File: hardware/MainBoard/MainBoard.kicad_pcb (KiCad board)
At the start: 2 copper layers, 38.1 x 73.8 mm, 50 parts, among them J1 Conn_01x08_Socket, J2 Conn_01x08_Socket, J3 Conn_01x08_Socket, J4 Micro_SD_Card_Det2, J5 USB_C_Receptacle_USB2.0_16P, J8 En_A, J9 En_B, Q1 MMBT2222A, U1 ESP32-S3-WROOM-1, U2 AMS1117-3.3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

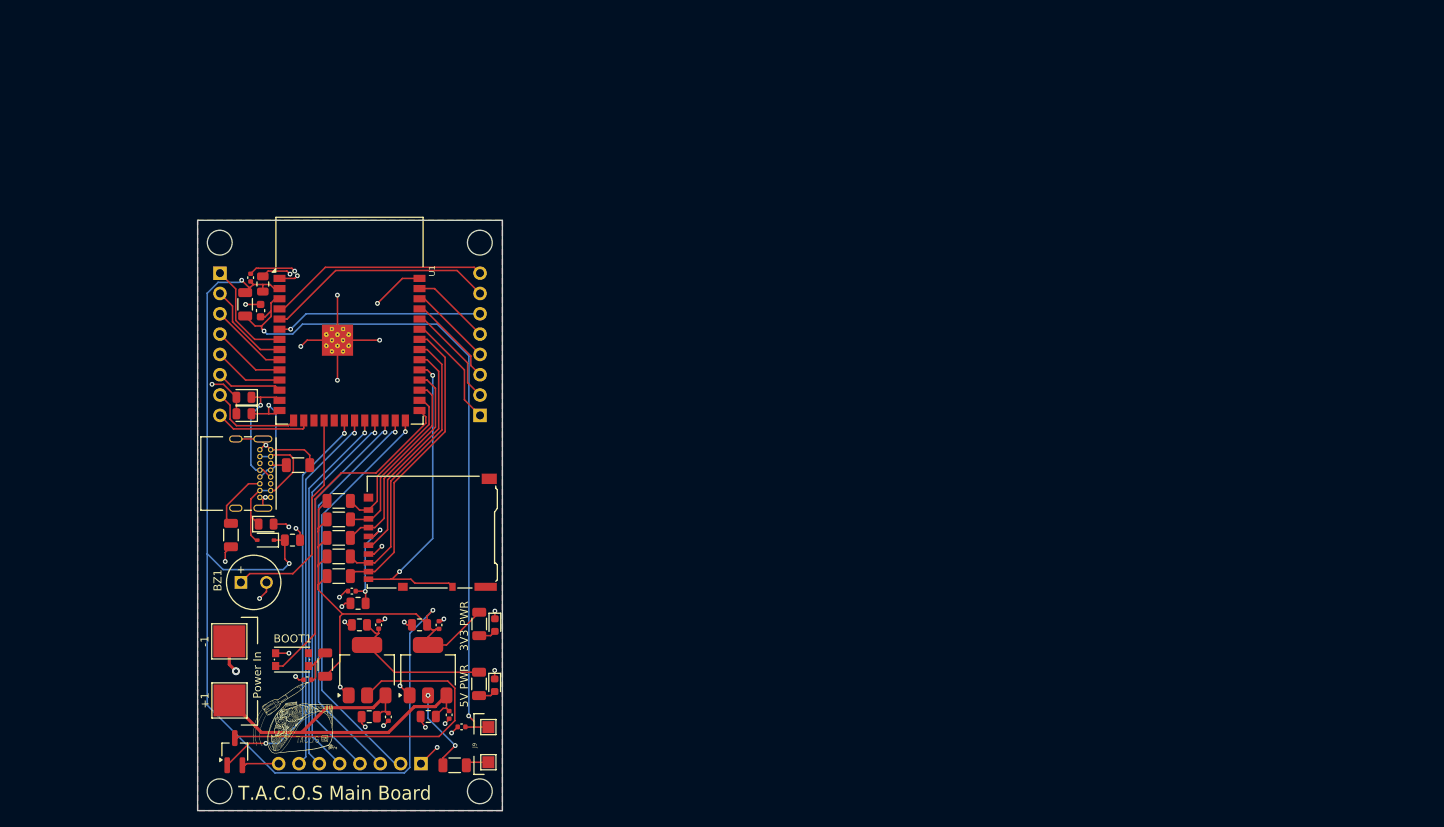
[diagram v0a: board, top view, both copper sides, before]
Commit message: designing new main board
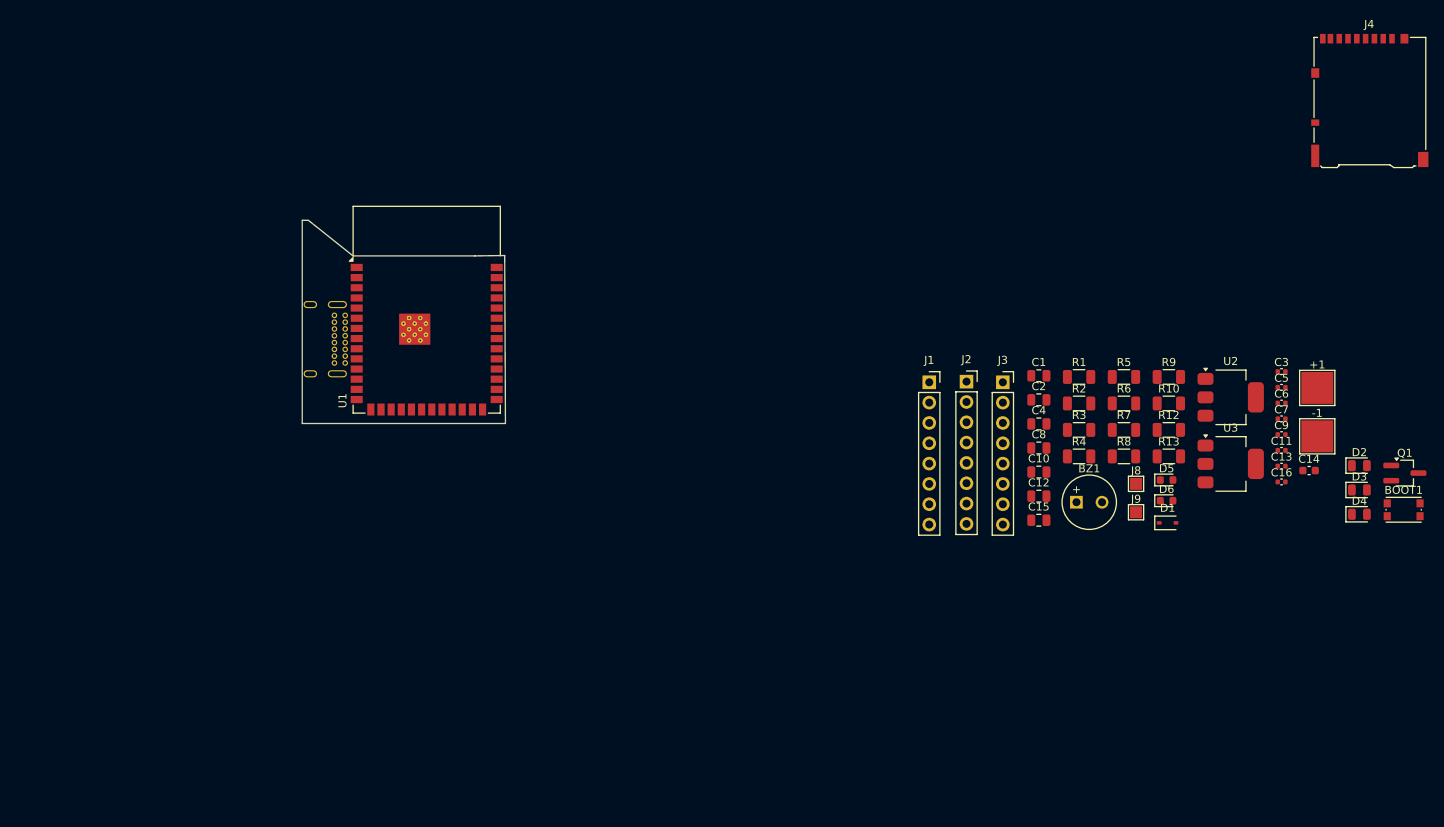
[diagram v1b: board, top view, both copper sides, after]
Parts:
- removed G***: LOGO, lib:tacos_logo
- J1, J2, J3: moved to F.Cu
- J5: moved to B.Cu
- moved Q1 150.3 mm to (201.7, 82.4), turned to 0 degrees
- moved +1 141.5 mm to (190.8, 71.8), turned to 0 degrees
- moved BOOT1 140.2 mm to (201.6, 87.0)
- moved D4 140.0 mm to (196.0, 87.5), turned to 0 degrees
- moved D3 139.9 mm to (196.0, 84.5), turned to 0 degrees
- moved -1 138.4 mm to (190.8, 77.8), turned to 0 degrees
- moved D2 136.9 mm to (196.0, 81.5)
- moved C14 132.6 mm to (189.7, 82.1), turned to 0 degrees
- moved C16 131.4 mm to (186.3, 83.5), turned to 0 degrees
- moved J4 129.2 mm to (197.3, 35.8), turned to 0 degrees
- moved C6 126.6 mm to (186.3, 73.7), turned to 0 degrees
- moved C13 117.3 mm to (186.3, 81.5), turned to 0 degrees
- moved C9 117.1 mm to (186.3, 77.6), turned to 0 degrees
- moved C11 115.0 mm to (186.3, 79.6), turned to 0 degrees
- moved D1 112.8 mm to (172.1, 88.6), turned to 0 degrees
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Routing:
- net ESP_3V3: track 211.4 -> 0.00 mm, vias 7 -> 0
- net LIPO GND: track 100.1 -> 0.00 mm, vias 36 -> 0
- net CHIP_PU: track 87.1 -> 0.00 mm, vias 2 -> 0
- net VCC_5V: track 64.5 -> 0.00 mm
- net HATS_ENABLE: track 52.0 -> 0.00 mm, vias 2 -> 0
- net I0: track 51.7 -> 0.00 mm, vias 1 -> 0
- net LIPO PWR: track 50.6 -> 0.00 mm
- net I1: track 50.3 -> 0.00 mm, vias 1 -> 0
- net I2: track 49.0 -> 0.00 mm, vias 1 -> 0
- net GPIO0: track 48.6 -> 0.00 mm
- net I3: track 47.8 -> 0.00 mm, vias 1 -> 0
- net I4: track 46.3 -> 0.00 mm, vias 1 -> 0
- net SELECT RETURN: track 46.0 -> 0.00 mm, vias 1 -> 0
- net SD_DET: track 40.6 -> 0.00 mm, vias 2 -> 0
- net SD_DAT1: track 37.8 -> 0.00 mm
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- removed copper zone on B.Cu, net LIPO GND
- removed copper zone on F.Cu, net LIPO GND
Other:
- board size 38.1 x 73.8 mm -> 25.4 x 25.4 mm
- board text removed: "3V3 PWR"
- board text removed: "5V PWR"
- board text removed: "Power In"
- board text removed: "T.A.C.O.S Main Board"

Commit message: main boards almost done:
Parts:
- removed J2, J3: Conn_01x08_Socket, Connector_PinSocket_2.54mm:PinSocket_1x08_P2.54mm_Vertical
- added Hat_Conn1: Conn_02x15_Top_Bottom, Connector_Molex:Molex_SlimStack_53748-0308_2x15_P0.50mm_Vertical, F.Cu at (82.8, 89.2)
- added Plug1: Conn_02x15_Top_Bottom, Connector_Molex:Molex_SlimStack_53748-0308_2x15_P0.50mm_Vertical, F.Cu at (80.3, 70.6)
- added Recepticle1: Conn_02x15_Top_Bottom, Connector_Molex:Molex_SlimStack_53748-0308_2x15_P0.50mm_Vertical, B.Cu at (80.3, 104.6)
- +1, -1: footprint TestPoint:TestPoint_Pad_4.0x4.0mm -> TestPoint:TestPoint_Pad_2.0x2.0mm; moved to B.Cu
- BOOT1, C11, C6, C7, C9, D5, J8, J9, U1, U3: moved to B.Cu
- BZ1: footprint Buzzer_Beeper:MagneticBuzzer_Kingstate_KCG0601 -> Buzzer_Beeper:Buzzer_Murata_PKMCS0909E; moved to B.Cu
- C1, C12, C15, C2, C4: footprint Capacitor_SMD:C_0805_2012Metric -> Capacitor_SMD:C_0603_1608Metric
- C10, C8: footprint Capacitor_SMD:C_0805_2012Metric -> Capacitor_SMD:C_0603_1608Metric; moved to B.Cu
- D2: footprint Diode_SMD:D_0805_2012Metric -> Diode_SMD:D_0603_1608Metric
- D3, D4: footprint Diode_SMD:D_0805_2012Metric -> Diode_SMD:D_0603_1608Metric; moved to B.Cu
- J1: value Conn_01x08_Socket -> Conn_01x01; footprint Connector_PinSocket_2.54mm:PinSocket_1x08_P2.54mm_Vertical -> TestPoint:TestPoint_Pad_1.5x1.5mm
- J5: moved to F.Cu
- Q1: footprint Package_TO_SOT_SMD:SOT-23W_Handsoldering -> Package_TO_SOT_SMD:SOT-23W; moved to B.Cu
- R1, R2: footprint Resistor_SMD:R_1206_3216Metric -> Resistor_SMD:R_0402_1005Metric
- R10, R12, R13, R4, R5, R6, R8, R9: footprint Resistor_SMD:R_1206_3216Metric -> Resistor_SMD:R_0603_1608Metric; moved to B.Cu
- R3, R7: footprint Resistor_SMD:R_1206_3216Metric -> Resistor_SMD:R_0603_1608Metric
- moved BOOT1 137.7 mm to (65.7, 64.6), turned to -90 degrees
- moved J4 133.1 mm to (81.4, 101.3)
- moved +1 129.3 mm to (65.7, 104.3), turned to 180 degrees
- moved -1 128.8 mm to (65.7, 108.4), turned to 180 degrees
- moved D3 128.5 mm to (69.0, 104.0), turned to 180 degrees
- moved D4 128.3 mm to (69.0, 105.7), turned to 180 degrees
- moved C14 126.2 mm to (65.5, 60.2), turned to 180 degrees
- moved Q1 125.8 mm to (77.2, 100.0), turned to 180 degrees
- moved D2 125.2 mm to (72.0, 98.6)
- moved C6 122.6 mm to (64.4, 60.8), turned to 90 degrees
- moved C7 121.0 mm to (65.3, 72.6), turned to 180 degrees
- moved C9 120.9 mm to (67.9, 101.8), turned to 90 degrees
- moved C11 116.0 mm to (70.8, 90.2), turned to 90 degrees
- moved C13 115.6 mm to (71.5, 95.5), turned to 180 degrees
- moved U3 113.2 mm to (67.6, 95.7), turned to 90 degrees
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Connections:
- net ESP_3V3 renamed CONN_26
- net HATS_ENABLE renamed CONN_12
- net SD_CLK renamed CONN_4
- net SD_CMD renamed CONN_6
- net SD_DAT0 renamed CONN_2
- net SD_DAT1 renamed CONN_0
- net SD_DAT2 renamed CONN_10
- net SD_DAT3 renamed CONN_8
- net USB+ renamed CONN_3
- net USB- renamed CONN_1
- J1 pad 1: LIPO GND -> CONN_5V
- Q1 pad 2: Net-(J1-Pin_8) -> CONN_5V
- U1 pad 10: DATA11 -> unconnected-(U1-IO17-Pad10)
- U1 pad 11: DATA12 -> unconnected-(U1-IO18-Pad11)
- U1 pad 12: DATA13 -> unconnected-(U1-IO8-Pad12)
- U1 pad 15: DATA14 -> unconnected-(U1-IO3-Pad15)
- U1 pad 16: DATA15 -> unconnected-(U1-IO46-Pad16)
- U1 pad 21: SELECT RETURN -> RET
- U1 pad 22: I4 -> unconnected-(U1-IO14-Pad22)
- U1 pad 23: I3 -> unconnected-(U1-IO21-Pad23)
- U1 pad 24: I2 -> unconnected-(U1-IO47-Pad24)
- U1 pad 25: I1 -> unconnected-(U1-IO48-Pad25)
- U1 pad 26: I0 -> unconnected-(U1-IO45-Pad26)
- U1 pad 35: DATA7 -> unconnected-(U1-IO42-Pad35)
- U1 pad 36: DATA6 -> unconnected-(U1-RXD0-Pad36)
- U1 pad 37: DATA5 -> unconnected-(U1-TXD0-Pad37)
- U1 pad 38: DATA4 -> unconnected-(U1-IO2-Pad38)
- U1 pad 39: DATA3 -> unconnected-(U1-IO1-Pad39)
- U1 pad 4: DATA0 -> unconnected-(U1-IO4-Pad4)
- U1 pad 5: DATA1 -> unconnected-(U1-IO5-Pad5)
- U1 pad 6: DATA2 -> unconnected-(U1-IO6-Pad6)
- U1 pad 7: DATA8 -> unconnected-(U1-IO7-Pad7)
- U1 pad 8: DATA9 -> unconnected-(U1-IO15-Pad8)
- U1 pad 9: DATA10 -> unconnected-(U1-IO16-Pad9)
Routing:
- net SD_DET: track 0.00 -> 10.9 mm, vias 0 -> 2
- net Net-(D6-A): track 0.00 -> 3.30 mm, vias 0 -> 1
- net LIPO GND: track 0.00 -> 3.10 mm, vias 0 -> 3
- net Net-(D5-A): track 0.00 -> 1.97 mm, vias 0 -> 1
- net CONN_3: track 0.00 -> 1.70 mm, vias 0 -> 1
- net CONN_1: track 0.00 -> 1.70 mm, vias 0 -> 1
- net CONN_0: track 0.00 -> 1.32 mm, vias 0 -> 2
- net CONN_4: track 0.00 -> 1.22 mm, vias 0 -> 2
- net CONN_26: track 0.00 -> 1.21 mm, vias 0 -> 6
- net CONN_2: track 0.00 -> 1.21 mm, vias 0 -> 2
- net CONN_8: track 0.00 -> 1.17 mm, vias 0 -> 2
- net CONN_6: track 0.00 -> 1.13 mm, vias 0 -> 2
- net CONN_10: track 0.00 -> 1.11 mm, vias 0 -> 2
- net (no net): track 0.00 -> 0.31 mm, vias 0 -> 20
- net unconnected-(U1-IO9-Pad17): vias 0 -> 1
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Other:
- board size 25.4 x 25.4 mm -> 25.4 x 59.4 mm

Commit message: started wiring main boards
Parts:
- removed the C1 at (65.6, 98.8)
- removed the C2 at (76.2, 67.1)
- removed the C3 at (78.5, 66.8)
- removed R13: 10k, Resistor_SMD:R_0603_1608Metric
- added C12: 10uF, Capacitor_SMD:C_0603_1608Metric, F.Cu at (65.6, 98.8)
- added C13: 10uF, Capacitor_SMD:C_0603_1608Metric, B.Cu at (77.4, 96.7)
- added C14: 0u1F, Capacitor_SMD:C_0402_1005Metric, B.Cu at (64.9, 59.6)
- added C15: 100nF, Capacitor_SMD:C_0402_1005Metric, B.Cu at (78.6, 97.2)
- added C16: 0u1F, Capacitor_SMD:C_0402_1005Metric, B.Cu at (65.3, 72.6)
- added G***: LOGO, lib:tacos_logo, F.Cu at (72.2, 81.1)
- added J10: Conn_01x01, TestPoint:TestPoint_Pad_1.5x1.5mm, B.Cu at (75.8, 104.6)
- added J2: Conn_01x01, TestPoint:TestPoint_Pad_1.5x1.5mm, F.Cu at (78.2, 89.1)
- added J3: USB_C_Receptacle_USB2.0_16P, Connector_USB:USB_C_Receptacle_GCT_USB4085, F.Cu at (72.5, 101.9)
- added J6: Micro_SD_Card_Det2, Connector_Card:microSD_HC_Hirose_DM3AT-SF-PEJM5, F.Cu at (81.4, 101.3)
- added J7: Conn_01x01, TestPoint:TestPoint_Pad_1.5x1.5mm, F.Cu at (85.1, 70.7)
- added R11: 10k, Resistor_SMD:R_0603_1608Metric, B.Cu at (86.1, 100.3)
- added R2: 75, Resistor_SMD:R_0603_1608Metric, F.Cu at (65.4, 56.3)
- added R7: 10k, Resistor_SMD:R_0603_1608Metric, B.Cu at (81.5, 100.3)
- C6: value 0u1F -> 10uF; footprint Capacitor_SMD:C_0402_1005Metric -> Capacitor_SMD:C_0603_1608Metric; moved to F.Cu
- C7, D3: moved to F.Cu
- D1: value 1N5819WS -> PWRLED; footprint Diode_SMD:D_SOD-323 -> LED_SMD:LED_0603_1608Metric; moved to B.Cu
- D2: value D_TVS_Small_Filled -> PWRLED; footprint Diode_SMD:D_0603_1608Metric -> LED_SMD:LED_0603_1608Metric
- D4: value D_TVS_Small_Filled -> 1N5819WS; footprint Diode_SMD:D_0603_1608Metric -> Diode_SMD:D_SOD-323; moved to F.Cu
- D5: value PWRLED -> D_TVS_Small_Filled; footprint LED_SMD:LED_0603_1608Metric -> Diode_SMD:D_0603_1608Metric
- D6: value PWRLED -> D_TVS_Small_Filled; footprint LED_SMD:LED_0603_1608Metric -> Diode_SMD:D_0603_1608Metric; moved to B.Cu
- J4: value Micro_SD_Card_Det2 -> En_A; footprint Connector_Card:microSD_HC_Hirose_DM3AT-SF-PEJM5 -> TestPoint:TestPoint_Pad_1.5x1.5mm; moved to B.Cu
- J5: value USB_C_Receptacle_USB2.0_16P -> En_B; footprint Connector_USB:USB_C_Receptacle_GCT_USB4085 -> TestPoint:TestPoint_Pad_1.5x1.5mm; moved to B.Cu
- J8: value En_A -> Conn_01x01; moved to F.Cu
- J9: value En_B -> Conn_01x01
- R3: moved to B.Cu
- R4, R5: value 10k -> 5k1; footprint Resistor_SMD:R_0603_1608Metric -> Resistor_SMD:R_0402_1005Metric
- R6: value 75 -> 10k
- moved D5 47.8 mm to (69.0, 104.0), turned to 180 degrees
- moved R4 46.9 mm to (68.4, 107.0), turned to 180 degrees
- moved R10 43.1 mm to (65.5, 60.9), turned to 180 degrees
- moved D1 42.4 mm to (65.4, 56.3)
- moved J9 35.9 mm to (84.9, 104.7)
- moved R12 35.6 mm to (65.5, 68.5), turned to 180 degrees
- moved J4 34.2 mm to (65.6, 70.9), turned to 180 degrees
- moved R5 33.9 mm to (68.4, 102.6)
- moved R3 33.9 mm to (65.7, 90.2), turned to 180 degrees
- moved J5 28.3 mm to (65.6, 74.4), turned to 180 degrees
- moved R6 20.0 mm to (83.0, 100.3), turned to -90 degrees
- moved D6 19.9 mm to (69.0, 105.7), turned to 180 degrees
- moved C7 18.6 mm to (79.2, 60.2), turned to 0 degrees
- moved C6 15.4 mm to (79.8, 61.5), turned to 0 degrees
- moved D2 14.4 mm to (64.7, 86.3), turned to -90 degrees
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- renumbered C14 to C1, C16 to C2, C15 to C3, R7 to R1
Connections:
- +1 pad 1: LIPO PWR -> CONN_3V
- C4 pad 1: CONN_26 -> CONN_3V
- C5 pad 1: CONN_26 -> CONN_3V
- C6 pad 1: GPIO0 -> CONN_26
- C7 pad 1: CHIP_PU -> CONN_26
- C8 pad 1: LIPO PWR -> CONN_3V
- C9 pad 1: LIPO PWR -> CONN_3V
- D1 pad 1: CONN_26 -> LIPO GND
- D2 pad 1: Net-(D1-A) -> LIPO GND
- D2 pad 2: LIPO GND -> Net-(D2-A)
- D3 pad 1: CONN_1 -> Net-(D3-A1)
- D4 pad 1: CONN_3 -> CONN_26
- D4 pad 2: LIPO GND -> Net-(D3-A1)
- D5 pad 1: LIPO GND -> CONN_1
- D5 pad 2: Net-(D5-A) -> LIPO GND
- D6 pad 1: LIPO GND -> CONN_3
- D6 pad 2: Net-(D6-A) -> LIPO GND
- Hat_Conn1 pad 30: unconnected-(Hat_Conn1-Pin_30-Pad30) -> RET
- J4 pad 1: CONN_10 -> Net-(J4-Pin_1)
- J8 pad 1: Net-(J8-Pin_1) -> CONN_GND
- J9 pad 1: CHIP_PU -> CONN_3V
- Plug1 pad 29: RET -> CONN_27
- R10 pad 2: CONN_6 -> GPIO0
- R12 pad 2: CONN_2 -> Net-(J4-Pin_1)
- R3 pad 1: CONN_26 -> VCC_5V
- R3 pad 2: Net-(D5-A) -> Net-(D2-A)
- R4 pad 1: CONN_26 -> Net-(J3-CC2)
- R4 pad 2: GPIO0 -> LIPO GND
- R5 pad 1: CONN_26 -> Net-(J3-CC1)
- R5 pad 2: Net-(J8-Pin_1) -> LIPO GND
- R6 pad 1: VCC_5V -> CONN_26
- R6 pad 2: Net-(D6-A) -> CONN_6
- R8 pad 2: CONN_10 -> CONN_8
- R9 pad 2: CONN_8 -> CONN_0
- U1 pad 27: GPIO0 -> unconnected-(U1-IO0-Pad27)
- U1 pad 39: unconnected-(U1-IO1-Pad39) -> GPIO0
- U2 pad 3: LIPO PWR -> CONN_3V
- U3 pad 3: LIPO PWR -> CONN_3V
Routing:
- net CONN_26: track 1.21 -> 30.5 mm, vias 6 -> 11
- net CHIP_PU: track 0.00 -> 28.8 mm
- net CONN_3V: track 0.00 -> 23.3 mm
- net GPIO0: track 0.00 -> 19.6 mm
- net LIPO GND: track 3.10 -> 15.8 mm, vias 3 -> 14
- net Net-(D6-A): track 3.30 -> 0.00 mm, vias 1 -> 0
- net Net-(D2-A): track 0.00 -> 1.98 mm, vias 0 -> 1
- net Net-(D5-A): track 1.97 -> 0.00 mm, vias 1 -> 0
- net Net-(D1-A): track 0.00 -> 1.97 mm, vias 0 -> 1
- net CONN_27: track 0.00 -> 1.60 mm, vias 0 -> 4
- net CONN_9: track 0.00 -> 0.82 mm, vias 0 -> 2
- net CONN_23: track 0.00 -> 0.82 mm, vias 0 -> 2
- net CONN_22: track 0.00 -> 0.82 mm, vias 0 -> 2
- net CONN_3: track 1.70 -> 2.51 mm, vias 1 -> 3
- net CONN_7: track 0.00 -> 0.81 mm, vias 0 -> 2
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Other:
- copper layers 2 -> 4

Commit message: wide board lel
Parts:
- removed Hat_Conn1, Plug1, Recepticle1: Conn_02x15_Top_Bottom, Connector_Molex:Molex_SlimStack_53748-0308_2x15_P0.50mm_Vertical
- removed J10, J8, J9: Conn_01x01, TestPoint:TestPoint_Pad_1.5x1.5mm
- J1: value Conn_01x01 -> Conn_02x16_Top_Bottom; footprint TestPoint:TestPoint_Pad_1.5x1.5mm -> MolexFSB:FSB5 Series 0.40 mm Pitch Floating SlimStack Board-to-Board Receptacles; moved to B.Cu
- J2, J7: value Conn_01x01 -> Conn_02x16_Top_Bottom; footprint TestPoint:TestPoint_Pad_1.5x1.5mm -> MolexFSB:FSB5 Series 0.40 mm Pitch Floating SlimStack Board-to-Board Plugs
- moved J7 19.3 mm to (80.3, 89.4)
- moved J2 18.6 mm to (80.3, 70.6), turned to 180 degrees
- moved J1 16.9 mm to (80.3, 104.6), turned to 180 degrees
- moved BZ1 0.20 mm to (83.9, 91.2)
- turned R11 to -90 degrees
- turned R8 to -90 degrees
- turned R9 to -90 degrees
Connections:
- -1 pad 1: LIPO GND -> CONN_GND
- BOOT1 pad 1: LIPO GND -> CONN_GND
- BZ1 pad 2: LIPO GND -> CONN_GND
- C1 pad 2: LIPO GND -> CONN_GND
- C10 pad 2: LIPO GND -> CONN_GND
- C11 pad 2: LIPO GND -> CONN_GND
- C12 pad 1: CONN_26 -> CONN_VCC
- C12 pad 2: LIPO GND -> CONN_GND
- C13 pad 1: CONN_26 -> CONN_VCC
- C13 pad 2: LIPO GND -> CONN_GND
- C14 pad 2: LIPO GND -> CONN_GND
- C15 pad 1: CONN_26 -> CONN_VCC
- C15 pad 2: LIPO GND -> CONN_GND
- C16 pad 2: LIPO GND -> CONN_GND
- C2 pad 1: CONN_26 -> CONN_VCC
- C2 pad 2: LIPO GND -> CONN_GND
- C3 pad 1: CONN_26 -> CONN_VCC
- C3 pad 2: LIPO GND -> CONN_GND
- C4 pad 2: LIPO GND -> CONN_GND
- C5 pad 2: LIPO GND -> CONN_GND
- C6 pad 1: CONN_26 -> CONN_VCC
- C6 pad 2: LIPO GND -> CONN_GND
- C7 pad 1: CONN_26 -> CONN_VCC
- C7 pad 2: LIPO GND -> CONN_GND
- C8 pad 2: LIPO GND -> CONN_GND
- C9 pad 2: LIPO GND -> CONN_GND
- D1 pad 1: LIPO GND -> CONN_GND
- D2 pad 1: LIPO GND -> CONN_GND
- D3 pad 2: LIPO GND -> CONN_GND
- D4 pad 1: CONN_26 -> CONN_VCC
- D5 pad 1: CONN_1 -> CONN_14
- D5 pad 2: LIPO GND -> CONN_GND
- D6 pad 1: CONN_3 -> CONN_15
- D6 pad 2: LIPO GND -> CONN_GND
- J1 pad 1: CONN_5V -> CONN_0
- J2 pad 1: CONN_GND -> CONN_16
- J3 pad A1: LIPO GND -> CONN_GND
- J3 pad A12: LIPO GND -> CONN_GND
- J3 pad A6: CONN_3 -> CONN_15
- J3 pad A7: CONN_1 -> CONN_14
- J3 pad B1: LIPO GND -> CONN_GND
- J3 pad B12: LIPO GND -> CONN_GND
- J3 pad B6: CONN_3 -> CONN_15
- J3 pad B7: CONN_1 -> CONN_14
- J3 pad S1: LIPO GND -> CONN_GND
- J6 pad 1: CONN_10 -> CONN_23
- J6 pad 11: LIPO GND -> CONN_GND
- J6 pad 2: CONN_8 -> CONN_24
- J6 pad 3: CONN_6 -> CONN_25
- J6 pad 4: CONN_26 -> CONN_VCC
- J6 pad 5: CONN_4 -> CONN_26
- J6 pad 6: LIPO GND -> CONN_GND
- J6 pad 7: CONN_2 -> CONN_27
- J6 pad 8: CONN_0 -> CONN_28
- J7 pad 1: CONN_3V -> unconnected-(J7-Pin_1-Pad1)
- R1 pad 1: CONN_26 -> CONN_VCC
- R10 pad 1: CONN_26 -> CONN_VCC
- R11 pad 1: CONN_26 -> CONN_VCC
- R11 pad 2: CONN_10 -> CONN_23
- R12 pad 1: CONN_26 -> CONN_VCC
- R2 pad 1: CONN_26 -> CONN_VCC
- R4 pad 2: LIPO GND -> CONN_GND
- R5 pad 2: LIPO GND -> CONN_GND
- R6 pad 1: CONN_26 -> CONN_VCC
- R6 pad 2: CONN_6 -> CONN_25
- R7 pad 1: CONN_26 -> CONN_VCC
- R7 pad 2: CONN_2 -> CONN_27
- R8 pad 1: CONN_26 -> CONN_VCC
- R8 pad 2: CONN_8 -> CONN_24
- R9 pad 1: CONN_26 -> CONN_VCC
- R9 pad 2: CONN_0 -> CONN_28
- U1 pad 1: LIPO GND -> CONN_GND
- U1 pad 13: CONN_1 -> CONN_14
- U1 pad 14: CONN_3 -> CONN_15
- U1 pad 2: CONN_26 -> CONN_VCC
- U1 pad 27: unconnected-(U1-IO0-Pad27) -> GPIO0
- U1 pad 28: CONN_10 -> CONN_23
- U1 pad 29: CONN_8 -> CONN_24
- U1 pad 30: CONN_6 -> CONN_25
- U1 pad 32: CONN_4 -> CONN_26
- U1 pad 33: CONN_2 -> CONN_27
- U1 pad 34: CONN_0 -> CONN_28
- U1 pad 38: unconnected-(U1-IO2-Pad38) -> CONN_4
- U1 pad 39: GPIO0 -> CONN_3
- U1 pad 40: LIPO GND -> CONN_GND
- U1 pad 41: LIPO GND -> CONN_GND
- U2 pad 1: LIPO GND -> CONN_GND
- U2 pad 2: CONN_26 -> CONN_VCC
- U3 pad 1: LIPO GND -> CONN_GND
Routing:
- net CONN_26: track 30.5 -> 0.00 mm, vias 11 -> 2
- net CONN_VCC: track 0.00 -> 28.9 mm, vias 0 -> 7
- net CONN_GND: track 0.00 -> 16.0 mm, vias 0 -> 14
- net LIPO GND: track 15.8 -> 0.00 mm, vias 14 -> 0
- net CONN_3V: track 23.3 -> 11.5 mm
- net GPIO0: track 19.6 -> 15.4 mm
- net CONN_1: track 2.49 -> 0.00 mm, vias 3 -> 0
- net CONN_3: track 2.51 -> 0.61 mm, vias 3 -> 1
- net CONN_27: track 1.60 -> 0.00 mm, vias 4 -> 2
- net CONN_15: track 0.79 -> 1.70 mm, vias 2 -> 1
- net CONN_14: track 0.79 -> 1.70 mm, vias 2 -> 1
- net CONN_9: track 0.82 -> 0.00 mm, vias 2 -> 0
- net CONN_8: track 0.82 -> 0.00 mm, vias 4 -> 0
- net CONN_23: track 0.82 -> 0.00 mm
- net CONN_22: track 0.82 -> 0.00 mm, vias 2 -> 0
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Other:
- board size 25.4 x 59.4 mm -> 28.6 x 59.4 mm
